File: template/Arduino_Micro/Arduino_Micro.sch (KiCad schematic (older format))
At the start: 6 parts, among them P1 Digital, P2 Analog, P3 CONN_1, P4 CONN_1, P5 CONN_1, P6 CONN_1

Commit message: Correction schématics
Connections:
- net labels added: 0(Rx1), 1(Tx1)
- net labels removed: 0(Rx), 1(Tx)
- wire segments 38 -> 39
- no-connect marks 2 -> 6
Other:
- note added: "Holes"
- moved on the sheet: P1, P2, P3, P4, P5, P6

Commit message: corrections
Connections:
- net labels removed: NC
- wire segments 39 -> 37
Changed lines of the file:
@@
 Text Label 10725 1950 0    60   ~ 0
 A5
-NoConn ~ 11100 1850
-NoConn ~ 11100 1750
+NoConn ~ 10325 1850
+NoConn ~ 10325 1750
 $Comp
 L GND #PWR01
@@
 Text Notes 8550 575  0    60   ~ 0
 Shield Arduino Micro Rev 3
-Text Label 10725 1750 0    60   ~ 0
-NC
-Text Label 10725 1850 0    60   ~ 0
-NC
 Text Notes 10875 925  0    60   ~ 0
 Holes
@@
 	10325 1550 11100 1550
 Wire Wire Line
-	10325 1750 11100 1750
-Wire Wire Line
-	10325 1850 11100 1850
-Wire Wire Line
 	10325 1950 11100 1950

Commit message: rebuilt shematic and fix librairie
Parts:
- removed P1: Digital, Socket_Arduino_Micro:Socket_Strip_Arduino_1x17, symbol CONN_17
- removed P2: Analog, Socket_Arduino_Micro:Socket_Strip_Arduino_1x17, symbol CONN_17
- removed P3, P4, P5, P6: CONN_1, Socket_Arduino_Micro:1pin_Micro, symbol CONN_1
- added P1: Digital, Socket_Arduino_Micro:Socket_Strip_Arduino_1x17, symbol CONN_01X17
- added P2: Analog, Socket_Arduino_Micro:Socket_Strip_Arduino_1x17, symbol CONN_01X17
- added P3, P4, P5, P6: CONN_01X01, Socket_Arduino_Micro:1pin_Micro, symbol CONN_01X01
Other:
- note added: "1"

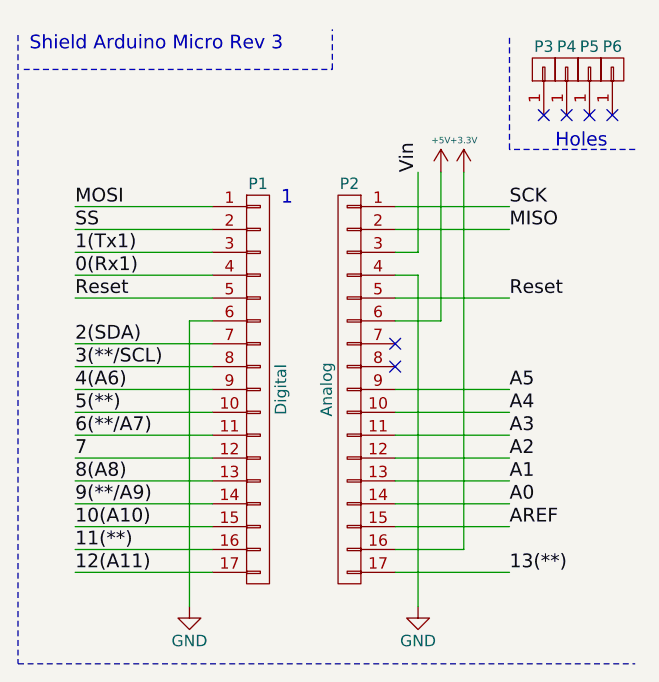
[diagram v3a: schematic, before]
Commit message: fix template
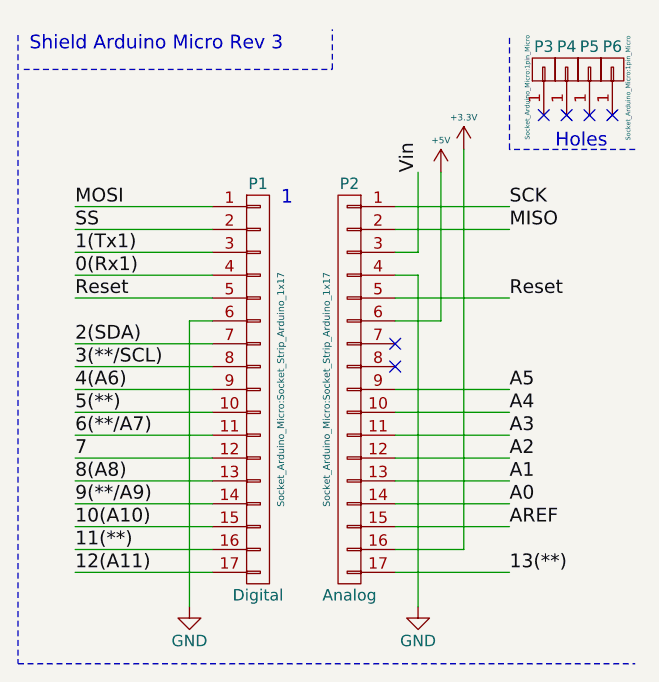
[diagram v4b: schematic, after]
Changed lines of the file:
@@
 P 9550 2050
 F 0 "P1" H 9550 2950 50  0000 C CNN
-F 1 "Digital" V 9650 2050 50  0000 C CNN
-F 2 "Socket_Arduino_Micro:Socket_Strip_Arduino_1x17" H 9550 2050 50  0001 C CNN
+F 1 "Digital" H 9550 1150 50  0000 C CNN
+F 2 "Socket_Arduino_Micro:Socket_Strip_Arduino_1x17" V 9650 2050 30  0000 C CNN
 F 3 "" H 9550 2050 50  0000 C CNN
 	1    9550 2050
@@
 P 9950 2050
 F 0 "P2" H 9950 2950 50  0000 C CNN
-F 1 "Analog" V 10050 2050 50  0000 C CNN
-F 2 "Socket_Arduino_Micro:Socket_Strip_Arduino_1x17" H 9950 2050 50  0001 C CNN
+F 1 "Analog" H 9950 1150 50  0000 C CNN
+F 2 "Socket_Arduino_Micro:Socket_Strip_Arduino_1x17" V 10050 2050 30  0000 C CNN
 F 3 "" H 9950 2050 50  0000 C CNN
 	1    9950 2050
@@
 L +3.3V #PWR04
 U 1 1 56D72867
-P 10450 1100
-F 0 "#PWR04" H 10450 950 50  0001 C CNN
-F 1 "+3.3V" H 10450 1240 28  0000 C CNN
-F 2 "" H 10450 1100 50  0000 C CNN
-F 3 "" H 10450 1100 50  0000 C CNN
-	1    10450 1100
+P 10450 1000
+F 0 "#PWR04" H 10450 850 50  0001 C CNN
+F 1 "+3.3V" H 10450 1140 28  0000 C CNN
+F 2 "" H 10450 1000 50  0000 C CNN
+F 3 "" H 10450 1000 50  0000 C CNN
+	1    10450 1000
 	1    0    0    -1
 $EndComp
@@
 	10250 1550 10250 3000
 Wire Wire Line
-	10450 1100 10450 2750
+	10450 1000 10450 2750
 Wire Wire Line
 	10450 2750 10150 2750
@@
 F 0 "P3" V 10900 650 50  0000 C CNN
 F 1 "CONN_01X01" H 10900 650 50  0001 C CNN
-F 2 "Socket_Arduino_Micro:1pin_Micro" H 10800 650 50  0001 C CNN
+F 2 "Socket_Arduino_Micro:1pin_Micro" H 10722 722 20  0000 C CNN
 F 3 "" H 10800 650 50  0000 C CNN
 	1    10800 650
@@
 F 0 "P4" V 11000 650 50  0000 C CNN
 F 1 "CONN_01X01" H 11000 650 50  0001 C CNN
-F 2 "Socket_Arduino_Micro:1pin_Micro" H 10900 650 50  0001 C CNN
+F 2 "Socket_Arduino_Micro:1pin_Micro" H 10900 650 20  0001 C CNN
 F 3 "" H 10900 650 50  0000 C CNN
 	1    10900 650
@@
 F 0 "P5" V 11100 650 50  0000 C CNN
 F 1 "CONN_01X01" H 11100 650 50  0001 C CNN
-F 2 "Socket_Arduino_Micro:1pin_Micro" H 11000 650 50  0001 C CNN
+F 2 "Socket_Arduino_Micro:1pin_Micro" H 11000 650 20  0001 C CNN
 F 3 "" H 11000 650 50  0000 C CNN
 	1    11000 650
@@
 F 0 "P6" V 11200 650 50  0000 C CNN
 F 1 "CONN_01X01" H 11200 650 50  0001 C CNN
-F 2 "Socket_Arduino_Micro:1pin_Micro" H 11100 650 50  0001 C CNN
+F 2 "Socket_Arduino_Micro:1pin_Micro" H 11019 581 20  0000 C CNN
 F 3 "" H 11100 650 50  0000 C CNN
 	1    11100 650
